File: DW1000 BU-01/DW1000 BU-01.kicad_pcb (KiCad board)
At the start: 2 copper layers, 26.5 x 40 mm, 17 parts, among them J1 Conn_01x10_Pin

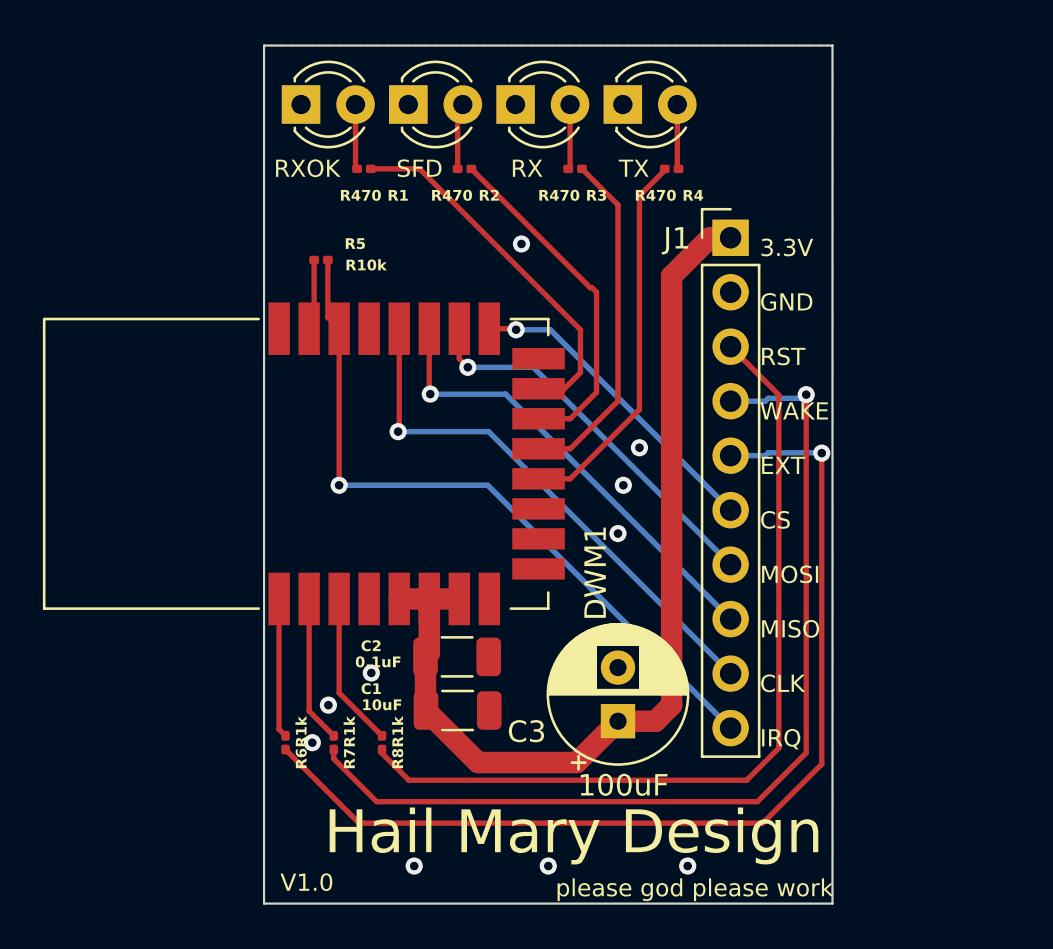
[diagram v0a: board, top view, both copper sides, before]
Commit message: cart remote pcb v2 update and follow me initial code
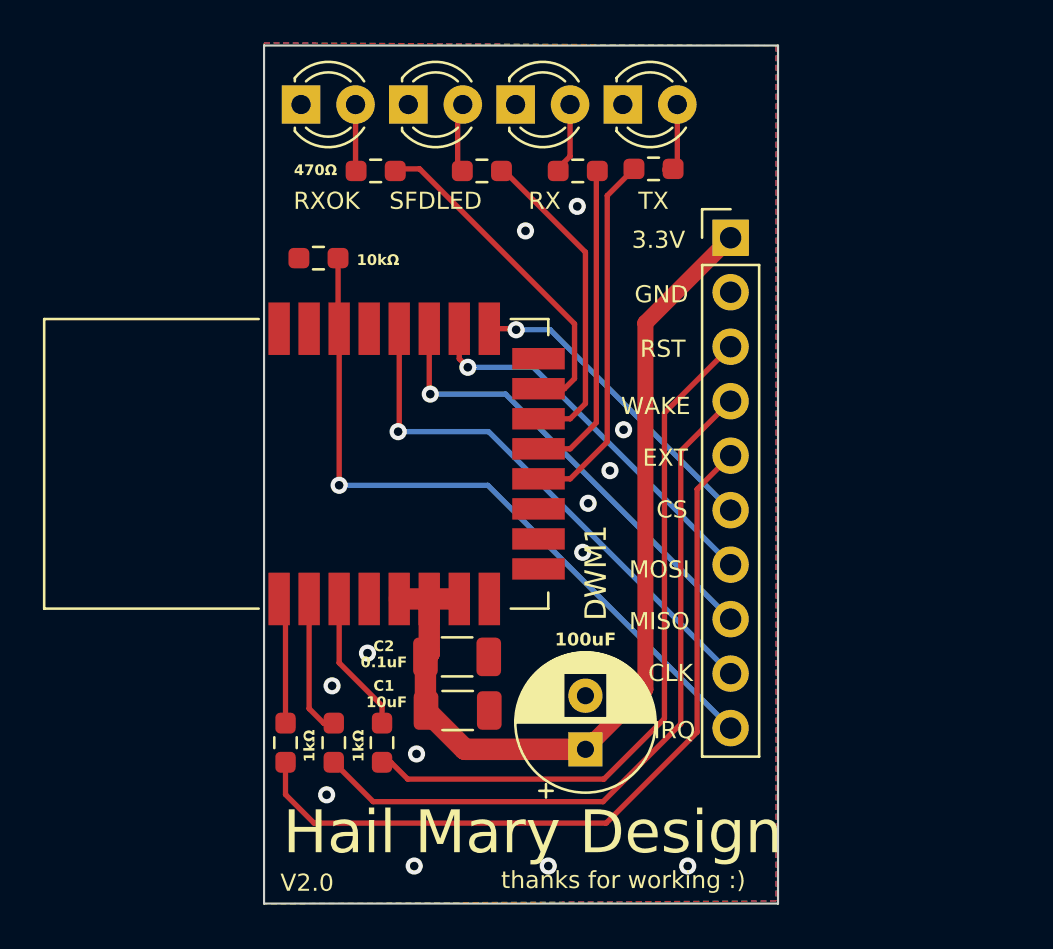
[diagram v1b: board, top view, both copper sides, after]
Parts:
- D2: value SFD -> SFDLED
- R1, R2, R3, R4, R5, R6, R7, R8: footprint Resistor_SMD:R_0201_0603Metric -> Resistor_SMD:R_0603_1608Metric_Pad0.98x0.95mm_HandSolder
- moved C3 2.00 mm to (14.7, 33.1)
- moved R4 0.84 mm to (17.9, 6.00)
- moved R2 0.82 mm to (9.91, 6.10)
- moved R1 0.56 mm to (4.95, 6.10)
- moved R3 0.16 mm to (14.4, 6.10)
- moved R5 0.15 mm to (2.29, 10.2)
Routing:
- net Net-(J1-Pin_4): track 44.6 -> 34.4 mm, vias 1 -> 0
- net Net-(J1-Pin_5): track 46.4 -> 36.5 mm, vias 1 -> 0
- net Net-(J1-Pin_3): track 39.5 -> 33.3 mm
- net GND: track 3.30 -> 0.33 mm, vias 10 -> 13
- net +3.3V: track 45.1 -> 42.9 mm
- net Net-(DWM1-GPIO0/RXOKLED): track 17.1 -> 15.8 mm
- net Net-(DWM1-GPIO2/RXLED): track 16.1 -> 15.1 mm
- net Net-(DWM1-GPIO1/SFDLED): track 16.1 -> 15.1 mm
- net Net-(DWM1-GPIO3/TXLED): track 17.8 -> 17.2 mm
- net RSTn: track 7.21 -> 6.62 mm
- net EXTON: track 6.50 -> 5.91 mm
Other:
- board size 26.5 x 40 mm -> 24 x 40 mm
- board text added: "10kΩ"
- board text added: "1kΩ"
- board text added: "470Ω"
- board text added: "V2.0"
- board text added: "thanks for working :)"
- board text removed: "V1.0"
- board text removed: "please god please work"
